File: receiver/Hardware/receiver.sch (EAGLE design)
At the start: 17 parts, among them IC2 MEGA8-P, Q1 16 MHz, X1 USB-A-H

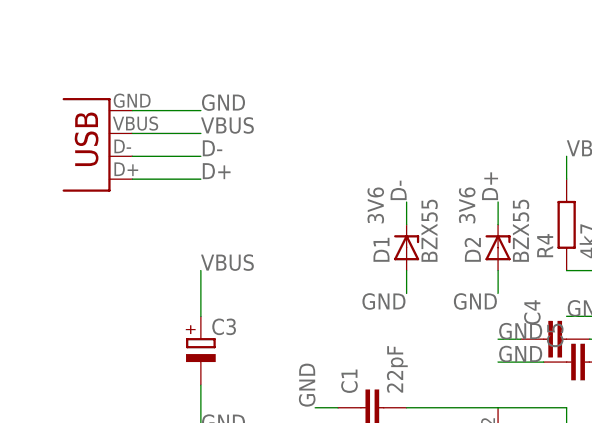
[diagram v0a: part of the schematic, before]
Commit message: Naprawa schematu
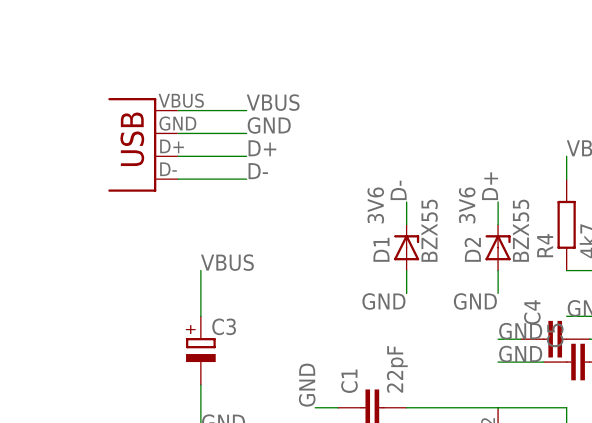
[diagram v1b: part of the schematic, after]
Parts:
- removed X1: USB-A-H, con-usb:USB-A-H
- added JP1: USB-A-H, SparkFun-Connectors:USB-A-H
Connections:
- net D+: now also JP1.D-; no longer X1.D+
- net D-: now also JP1.D+; no longer X1.D-
- net GND: now also JP1.VBUS; no longer X1.GND
- net VBUS: now also JP1.GND; no longer X1.VBUS
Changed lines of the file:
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@@
 <part name="C6" library="rcl" deviceset="C-EU" device="050-024X044"/>
 <part name="TSOP1" library="tsop" deviceset="TSOP1730" device=""/>
-<part name="X1" library="con-usb" deviceset="USB" device="-A-H"/>
+<part name="JP1" library="SparkFun-Connectors" deviceset="USB" device="-A-H"/>
 </parts>
 <sheets>
@@
 <instance part="C6" gate="G$1" x="50.8" y="25.4" rot="R90"/>
 <instance part="TSOP1" gate="G$1" x="127" y="81.28" rot="R180"/>
-<instance part="X1" gate="G$1" x="0" y="78.74" rot="R180"/>
+<instance part="JP1" gate="G$1" x="5.08" y="78.74" rot="R180"/>
 </instances>
 <busses>
@@
 </segment>
 <segment>
-<pinref part="X1" gate="G$1" pin="GND"/>
-<wire x1="2.54" y1="78.74" x2="10.16" y2="78.74" width="0.1524" layer="91"/>
-<label x="10.16" y="78.74" size="1.778" layer="95"/>
+<pinref part="JP1" gate="G$1" pin="VBUS"/>
+<wire x1="7.62" y1="76.2" x2="15.24" y2="76.2" width="0.1524" layer="91"/>
+<label x="15.24" y="76.2" size="1.778" layer="95"/>
 </segment>
 </net>
@@
 </segment>
 <segment>
-<pinref part="X1" gate="G$1" pin="VBUS"/>
-<wire x1="2.54" y1="76.2" x2="10.16" y2="76.2" width="0.1524" layer="91"/>
-<label x="10.16" y="76.2" size="1.778" layer="95"/>
+<pinref part="JP1" gate="G$1" pin="GND"/>
+<wire x1="7.62" y1="78.74" x2="15.24" y2="78.74" width="0.1524" layer="91"/>
+<label x="15.24" y="78.74" size="1.778" layer="95"/>
 </segment>
 </net>
@@
 </segment>
 <segment>
-<pinref part="X1" gate="G$1" pin="D-"/>
-<wire x1="2.54" y1="73.66" x2="10.16" y2="73.66" width="0.1524" layer="91"/>
-<label x="10.16" y="73.66" size="1.778" layer="95"/>
+<pinref part="JP1" gate="G$1" pin="D+"/>
+<wire x1="7.62" y1="71.12" x2="15.24" y2="71.12" width="0.1524" layer="91"/>
+<label x="15.24" y="71.12" size="1.778" layer="95"/>
 </segment>
 </net>
@@
 </segment>
 <segment>
-<pinref part="X1" gate="G$1" pin="D+"/>
-<wire x1="2.54" y1="71.12" x2="10.16" y2="71.12" width="0.1524" layer="91"/>
-<label x="10.16" y="71.12" size="1.778" layer="95"/>
+<pinref part="JP1" gate="G$1" pin="D-"/>
+<wire x1="7.62" y1="73.66" x2="15.24" y2="73.66" width="0.1524" layer="91"/>
+<label x="15.24" y="73.66" size="1.778" layer="95"/>
 </segment>
 </net>
